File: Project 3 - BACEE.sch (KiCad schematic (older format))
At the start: 0 parts

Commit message: Create new child scheet, added project symbols.
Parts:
- added BT?: Battery, symbol Device:Battery
- added C? (x2): C, symbol Device:C
- added C?: CP, symbol Device:CP
- added D?: LED, symbol Device:LED
- added R? (x2): R, symbol Device:R
- added U?: 24LC1025, symbol Memory_EEPROM:24LC1025
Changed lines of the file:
@@
 $Descr A4 11693 8268
 encoding utf-8
-Sheet 1 1
+Sheet 1 2
 Title "Battery Power Arduino clone with clock and Extended EEPROM"
 Date "2020-07-11"
@@
 Comment4 ""
 $EndDescr
+$Comp
+L Device:Battery BT?
+U 1 1 5F0CDB03
+P 2500 3050
+F 0 "BT?" H 2608 3096 50  0000 L CNN
+F 1 "Battery" H 2608 3005 50  0000 L CNN
+F 2 "" V 2500 3110 50  0001 C CNN
+F 3 "~" V 2500 3110 50  0001 C CNN
+	1    2500 3050
+	1    0    0    -1
+$EndComp
+$Comp
+L Device:C C?
+U 1 1 5F0CEA38
+P 3175 2900
+F 0 "C?" H 3290 2946 50  0000 L CNN
+F 1 "C" H 3290 2855 50  0000 L CNN
+F 2 "" H 3213 2750 50  0001 C CNN
+F 3 "~" H 3175 2900 50  0001 C CNN
+	1    3175 2900
+	1    0    0    -1
+$EndComp
+$Comp
+L Device:C C?
+U 1 1 5F0CF2D4
+P 3175 3375
+F 0 "C?" H 3290 3421 50  0000 L CNN
+F 1 "C" H 3290 3330 50  0000 L CNN
+F 2 "" H 3213 3225 50  0001 C CNN
+F 3 "~" H 3175 3375 50  0001 C CNN
+	1    3175 3375
+	1    0    0    -1
+$EndComp
+$Comp
+L Device:CP C?
+U 1 1 5F0CF8DC
+P 3175 3875
+F 0 "C?" H 3293 3921 50  0000 L CNN
+F 1 "CP" H 3293 3830 50  0000 L CNN
+F 2 "" H 3213 3725 50  0001 C CNN
+F 3 "~" H 3175 3875 50  0001 C CNN
+	1    3175 3875
+	1    0    0    -1
+$EndComp
+$Comp
+L Device:LED D?
+U 1 1 5F0CFE76
+P 2500 3675
+F 0 "D?" H 2493 3892 50  0000 C CNN
+F 1 "LED" H 2493 3801 50  0000 C CNN
+F 2 "" H 2500 3675 50  0001 C CNN
+F 3 "~" H 2500 3675 50  0001 C CNN
+	1    2500 3675
+	1    0    0    -1
+$EndComp
+$Comp
+L Device:R R?
+U 1 1 5F0D09EF
+P 3800 2900
+F 0 "R?" H 3870 2946 50  0000 L CNN
+F 1 "R" H 3870 2855 50  0000 L CNN
+F 2 "" V 3730 2900 50  0001 C CNN
+F 3 "~" H 3800 2900 50  0001 C CNN
+	1    3800 2900
+	1    0    0    -1
+$EndComp
+$Comp
+L Device:R R?
+U 1 1 5F0D11B8
+P 3800 3375
+F 0 "R?" H 3870 3421 50  0000 L CNN
+F 1 "R" H 3870 3330 50  0000 L CNN
+F 2 "" V 3730 3375 50  0001 C CNN
+F 3 "~" H 3800 3375 50  0001 C CNN
+	1    3800 3375
+	1    0    0    -1
+$EndComp
+$Comp
+L Memory_EEPROM:24LC1025 U?
+U 1 1 5F0D1B59
+P 4800 2900
+F 0 "U?" H 4800 3381 50  0000 C CNN
+F 1 "24LC1025" H 4800 3290 50  0000 C CNN
+F 2 "" H 4800 2900 50  0001 C CNN
+F 3 "http://ww1.microchip.com/downloads/en/DeviceDoc/21941B.pdf" H 4800 2900 50  0001 C CNN
+	1    4800 2900
+	1    0    0    -1
+$EndComp
+$Sheet
+S 5475 4075 1150 1800
+U 5F0D3531
+F0 "Connectors" 50
+F1 "Connectors.sch" 50
+$EndSheet
 $EndSCHEMATC

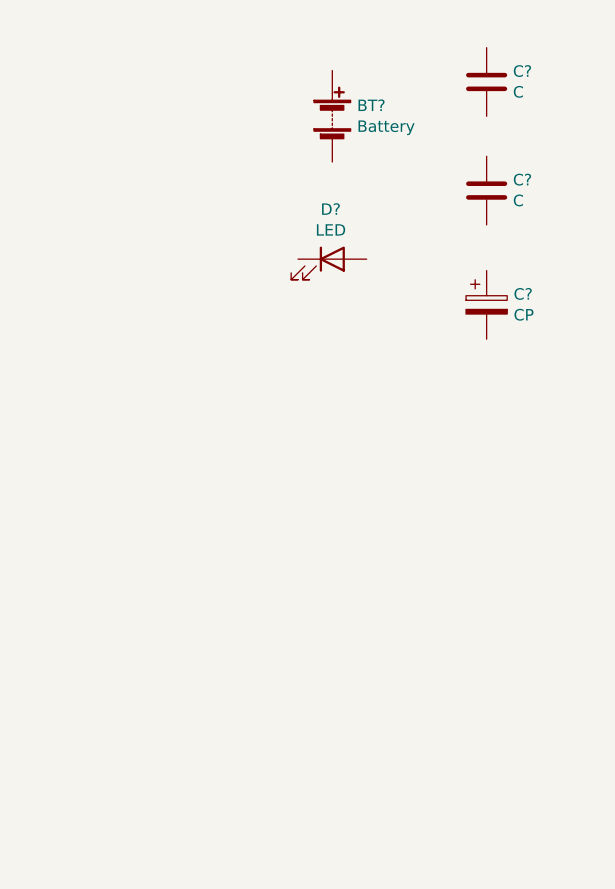
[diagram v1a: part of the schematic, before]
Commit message: Added symbol for ATMEGA328P-AU
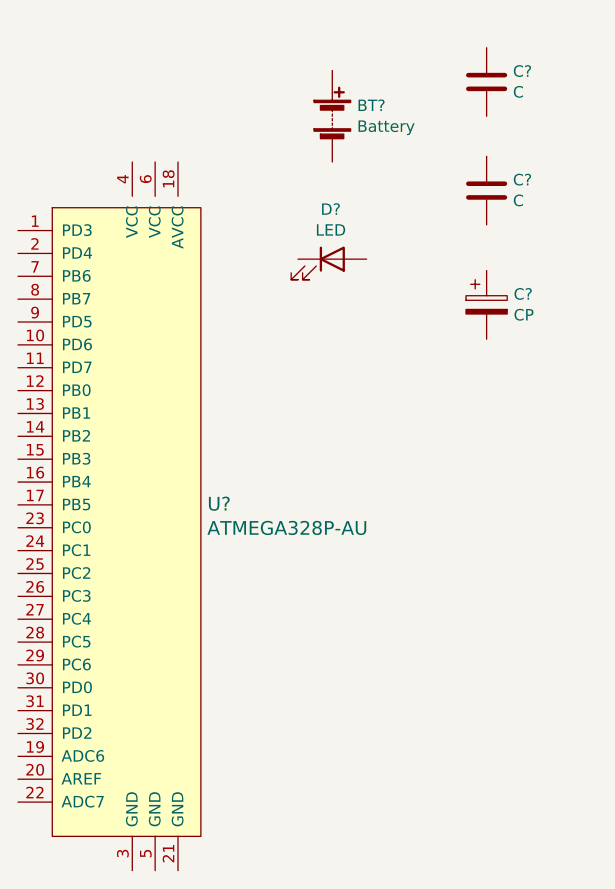
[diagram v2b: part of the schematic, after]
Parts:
- added U?: ATMEGA328P-AU, digikey-footprints:TQFP-32_7x7mm, symbol dk_Embedded-Microcontrollers:ATMEGA328P-AU
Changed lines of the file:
@@
 F1 "Connectors.sch" 50
 $EndSheet
+$Comp
+L dk_Embedded-Microcontrollers:ATMEGA328P-AU U?
+U 1 1 5F0D825C
+P 1625 4850
+F 0 "U?" H 1953 4953 60  0000 L CNN
+F 1 "ATMEGA328P-AU" H 1953 4847 60  0000 L CNN
+F 2 "digikey-footprints:TQFP-32_7x7mm" H 1825 5050 60  0001 L CNN
+F 3 "http://www.microchip.com/mymicrochip/filehandler.aspx?ddocname=en608326" H 1825 5150 60  0001 L CNN
+F 4 "ATMEGA328P-AU-ND" H 1825 5250 60  0001 L CNN "Digi-Key_PN"
+F 5 "ATMEGA328P-AU" H 1825 5350 60  0001 L CNN "MPN"
+F 6 "Integrated Circuits (ICs)" H 1825 5450 60  0001 L CNN "Category"
+F 7 "Embedded - Microcontrollers" H 1825 5550 60  0001 L CNN "Family"
+F 8 "http://www.microchip.com/mymicrochip/filehandler.aspx?ddocname=en608326" H 1825 5650 60  0001 L CNN "DK_Datasheet_Link"
+F 9 "/product-detail/en/microchip-technology/ATMEGA328P-AU/ATMEGA328P-AU-ND/1832260" H 1825 5750 60  0001 L CNN "DK_Detail_Page"
+F 10 "IC MCU 8BIT 32KB FLASH 32TQFP" H 1825 5850 60  0001 L CNN "Description"
+F 11 "Microchip Technology" H 1825 5950 60  0001 L CNN "Manufacturer"
+F 12 "Active" H 1825 6050 60  0001 L CNN "Status"
+	1    1625 4850
+	1    0    0    -1
+$EndComp
 $EndSCHEMATC

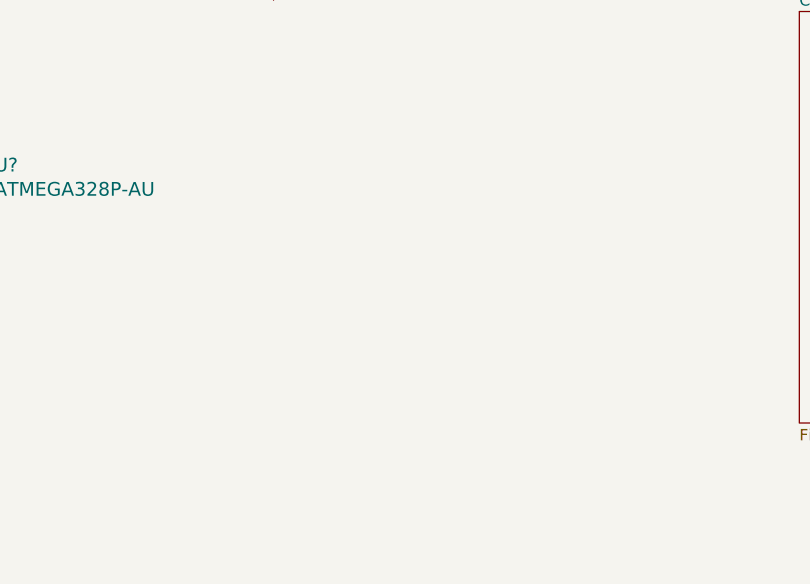
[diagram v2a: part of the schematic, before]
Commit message: Added clock IC custom symbol
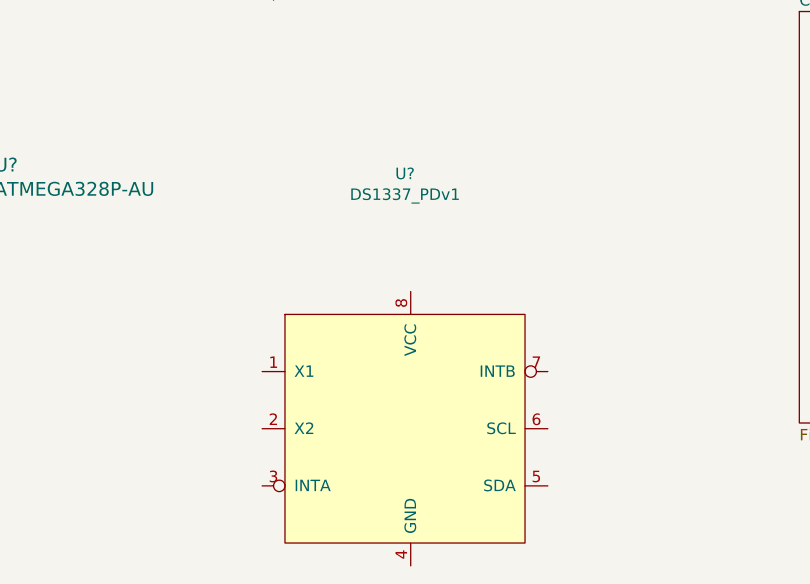
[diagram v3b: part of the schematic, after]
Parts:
- added U?: DS1337_PDv1, symbol Project3:DS1337_PDv1
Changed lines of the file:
@@
+	1    0    0    -1
+$EndComp
+$Comp
+L Project3:DS1337_PDv1 U?
+U 1 1 5F0DBCFF
+P 3775 5900
+F 0 "U?" H 3750 7015 50  0000 C CNN
+F 1 "DS1337_PDv1" H 3750 6924 50  0000 C CNN
+F 2 "" H 3475 6250 50  0001 C CNN
+F 3 "https://datasheets.maximintegrated.com/en/ds/DS1337-DS1337C.pdf" H 3475 6250 50  0001 C CNN
+	1    3775 5900
 	1    0    0    -1
 $EndComp
